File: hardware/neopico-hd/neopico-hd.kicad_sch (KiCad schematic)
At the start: 25 parts, among them J1 HDMI_A, J2 Conn_02x05_Top_Bottom, J4 Audio, J5 AUX, J6 Conn_01x02_Pin, SW1 MENU, SW2 BACK, U1 A_BUFF, U2 V_BUFF, U3 RG_LVS, U4 GB_LVS, U5 AV_LVS

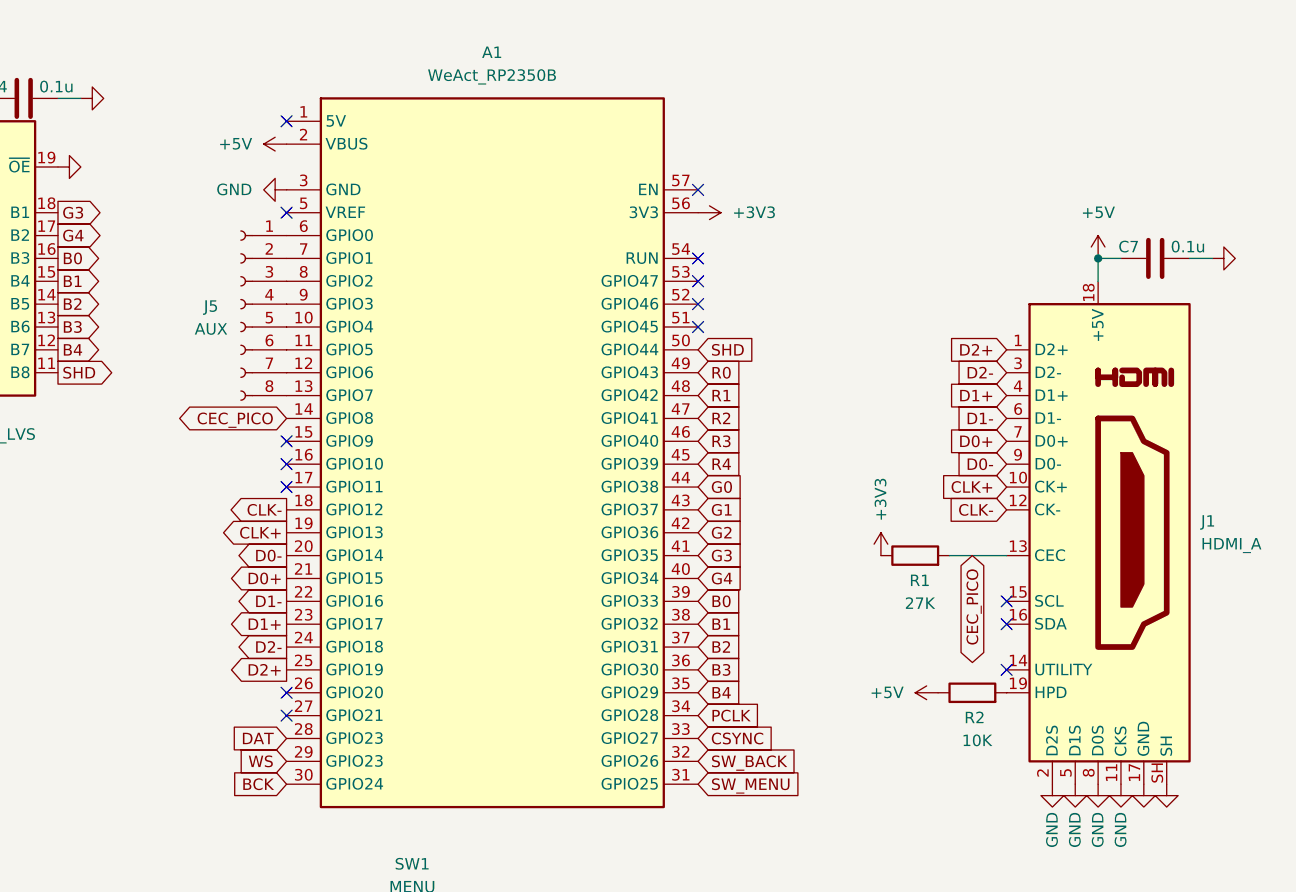
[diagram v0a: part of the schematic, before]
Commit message: Hardware - add HDMI termination resistors and more
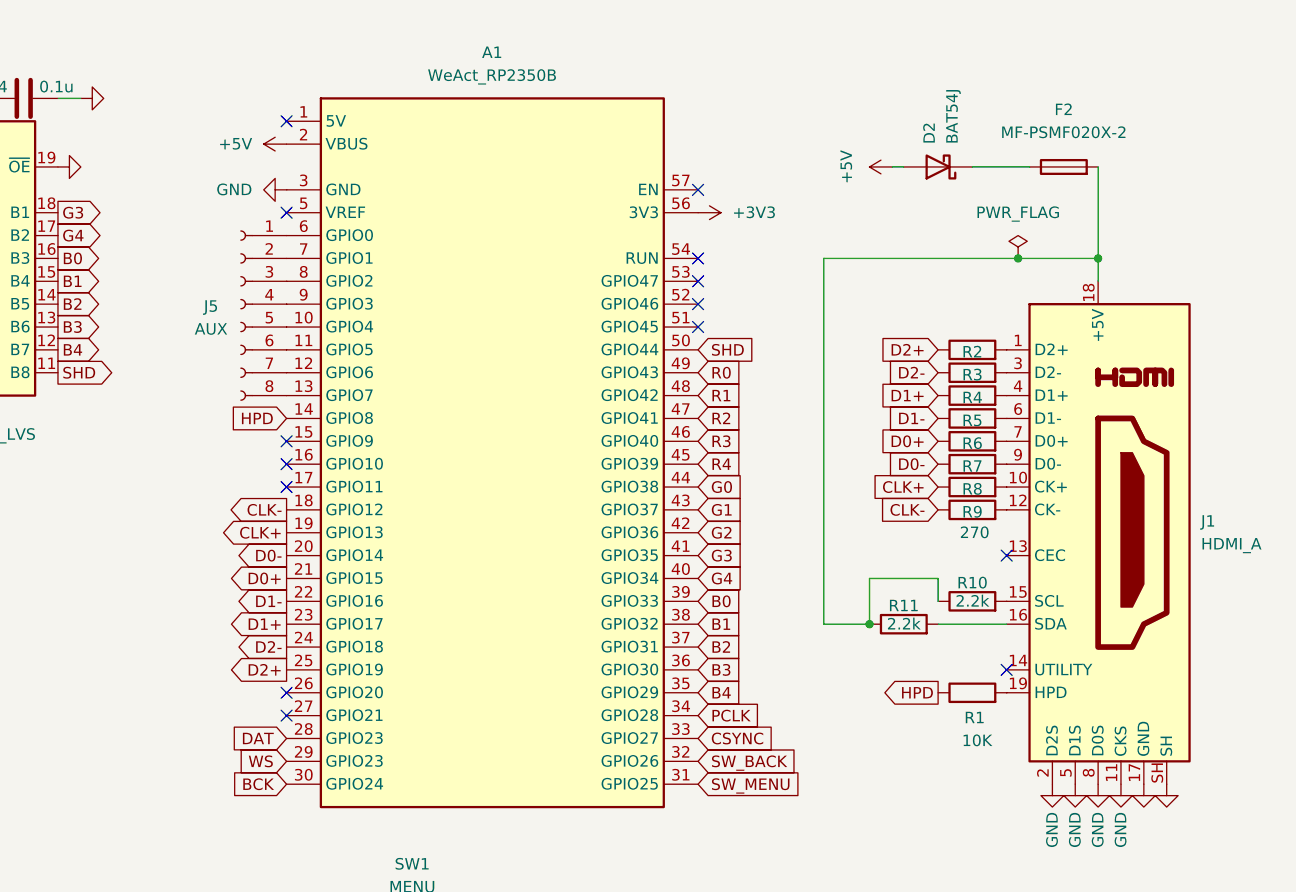
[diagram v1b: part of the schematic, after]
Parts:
- removed C7: 0.1u, Capacitor_SMD:C_0805_2012Metric_Pad1.18x1.45mm_HandSolder, symbol Device:C
- removed R1: 27K, Resistor_SMD:R_0805_2012Metric, symbol Device:R
- added D2: BAT54J, Diode_SMD:D_SOD-323F, symbol Diode:BAT54J
- added F2: MF-PSMF020X-2, Fuse:Fuse_0805_2012Metric, symbol Device:Fuse
- added R10, R11: 2.2k, Resistor_SMD:R_0603_1608Metric, symbol Device:R
- added R2, R3, R4, R5, R6, R7, R8, R9: 270, Resistor_SMD:R_0402_1005Metric, symbol Device:R
- R1: renamed from R2; footprint Resistor_SMD:R_0805_2012Metric_Pad1.20x1.40mm_HandSolder -> Resistor_SMD:R_0603_1608Metric
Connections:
- net +5V: now also D2.2 (A); no longer J1.18 (+5V), R1.1
- net CLK+: now also R8.1; no longer J1.10 (CK+)
- net CLK-: now also R9.1; no longer J1.12 (CK-)
- net D0+: now also R6.1; no longer J1.7 (D0+)
- net D0-: now also R7.1; no longer J1.9 (D0-)
- net D1+: now also R4.1; no longer J1.4 (D1+)
- net D1-: now also R5.1; no longer J1.6 (D1-)
- net D2+: now also R2.1; no longer J1.1 (D2+)
- net D2-: now also R3.1; no longer J1.3 (D2-)
- net at J1.15 (SCL): now also R10.2
- net at J1.16 (SDA): now also R11.2
- net CEC_PICO: no longer names the net of J1.13 (CEC)
- net CEC_PICO: no longer A1.14 (GPIO8)
- new net: J1.10 (CK+), R8.2
- new net: F2.2, J1.18 (+5V), R10.1, R11.1
- new net: J1.1 (D2+), R2.2
- new net: J1.6 (D1-), R5.2
- new net: D2.1 (K), F2.1
- new net: J1.9 (D0-), R7.2
- new net: J1.4 (D1+), R4.2
- new net: J1.7 (D0+), R6.2
- new net: J1.12 (CK-), R9.2
- new net: J1.3 (D2-), R3.2
- new net HPD: A1.14 (GPIO8), R1.1
- no-connect marks 31 -> 30

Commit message: Minor hardware tweaks
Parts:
- C6: footprint Capacitor_THT:CP_Radial_D5.0mm_P2.00mm -> Capacitor_SMD:CP_Elec_6.3x5.4_Nichicon
- D1: LCSC (none) -> C83852
- D2: LCSC (none) -> C86299
- F1: value Polyfuse -> MF-PSMF020X-2; symbol Device:Polyfuse -> Device:Fuse; LCSC (none) -> C89657
- F2: LCSC (none) -> C89657
- FB1: LCSC (none) -> C76815
- J4: footprint Connector_JST:JST_XA_B03B-XASK-1_1x03_P2.50mm_Vertical -> Connector_JST:JST_XA_B04B-XASK-1_1x04_P2.50mm_Vertical; symbol Connector_Generic:Conn_01x03 -> Connector_Generic:Conn_01x04
- R1: LCSC (none) -> C98220
- R10, R11: LCSC (none) -> C114662
- R2, R3, R4, R5, R6, R7, R8, R9: LCSC (none) -> C163474
- SW1, SW2: footprint Connector_Samtec_HPM_THT:Samtec_HPM-02-01-x-S_Straight_1x02_Pitch5.08mm -> Button_Switch_SMD:SW_SPST_CK_KXT3
- U1: value A_BUFF -> SN74LVC2G14DBV; LCSC (none) -> C12401
- U2: value V_BUFF -> SN74LVC2G14DBV; LCSC (none) -> C12401
- U3: value RG_LVS -> SN74LVC245APW; LCSC (none) -> C7848
- U4: value GB_LVS -> SN74LVC245APW; LCSC (none) -> C7848
- U5: value AV_LVS -> SN74LVC245APW; LCSC (none) -> C7848
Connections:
- net GND: now also J2.20 (Pin_20), J4.1 (Pin_1)
- net MVS_BCK: now also J4.2 (Pin_2); no longer J4.1 (Pin_1)
- net MVS_DAT: now also J4.4 (Pin_4); no longer J4.3 (Pin_3)
- net MVS_WS: now also J4.3 (Pin_3); no longer J4.2 (Pin_2)
- net MVS_DARK: now reaches J2.17 (Pin_17)
- net MVS_DARK: now also A1.51 (GPIO45)
- no-connect marks 30 -> 27

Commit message: Update PCB
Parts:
- A1, J2, J4, J5, J6, SW1, SW2: now left out of the parts list
- C1, C2, C3, C4, C5: LCSC (none) -> C1711
- C6: LCSC (none) -> C7094687
- J1: LCSC (none) -> C111617; now left out of the parts list
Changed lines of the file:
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@@
 			)
 		)
+		(property "LCSC" "C1711"
+			(at 100.33 66.04 90)
+			(effects
+				(font
+					(size 1.27 1.27)
+				)
+				(hide yes)
+			)
+		)
 		(pin "1"
 		)
@@
 		(unit 1)
 		(exclude_from_sim no)
-		(in_bom yes)
+		(in_bom no)
 		(on_board yes)
 		(dnp no)
@@
 			)
 		)
+		(property "LCSC" "C1711"
+			(at 52.07 91.44 90)
+			(effects
+				(font
+					(size 1.27 1.27)
+				)
+				(hide yes)
+			)
+		)
 		(pin "1"
 		)
@@
 			)
 		)
+		(property "LCSC" "C7094687"
+			(at 73.66 179.07 0)
+			(effects
+				(font
+					(size 1.27 1.27)
+				)
+				(hide yes)
+			)
+		)
 		(pin "1"
 		)
@@
 		(unit 1)
 		(exclude_from_sim no)
-		(in_bom yes)
+		(in_bom no)
 		(on_board yes)
 		(dnp no)
@@
 		(unit 1)
 		(exclude_from_sim no)
-		(in_bom yes)
+		(in_bom no)
 		(on_board yes)
 		(dnp no)
@@
 			)
 		)
+		(property "LCSC" "C1711"
+			(at 100.33 96.52 90)
+			(effects
+				(font
+					(size 1.27 1.27)
+				)
+				(hide yes)
+			)
+		)
 		(pin "1"
 		)
@@
 			)
 		)
+		(property "LCSC" "C1711"
+			(at 96.52 21.59 90)
+			(effects
+				(font
+					(size 1.27 1.27)
+				)
+				(hide yes)
+			)
+		)
 		(pin "1"
 		)
@@
 			)
 		)
+		(property "LCSC" "C1711"
+			(at 144.78 21.59 90)
+			(effects
+				(font
+					(size 1.27 1.27)
+				)
+				(hide yes)
+			)
+		)
 		(pin "1"
 		)
@@
 		(unit 1)
 		(exclude_from_sim no)
-		(in_bom yes)
+		(in_bom no)
 		(on_board yes)
 		(dnp no)
@@
 		(unit 1)
 		(exclude_from_sim no)
-		(in_bom yes)
+		(in_bom no)
 		(on_board yes)
 		(dnp no)
@@
 		(unit 1)
 		(exclude_from_sim no)
-		(in_bom yes)
+		(in_bom no)
 		(on_board yes)
 		(dnp no)
@@
 		(unit 1)
 		(exclude_from_sim no)
-		(in_bom yes)
+		(in_bom no)
 		(on_board yes)
 		(dnp no)
@@
 		(unit 1)
 		(exclude_from_sim no)
-		(in_bom yes)
+		(in_bom no)
 		(on_board yes)
 		(dnp no)
@@
 			(at 264.16 69.85 0)
 			(effects
+				(font
+					(size 1.27 1.27)
+				)
+				(hide yes)
+			)
+		)
+		(property "LCSC" "C111617"
+			(at 264.16 69.85 0)
+			(effects

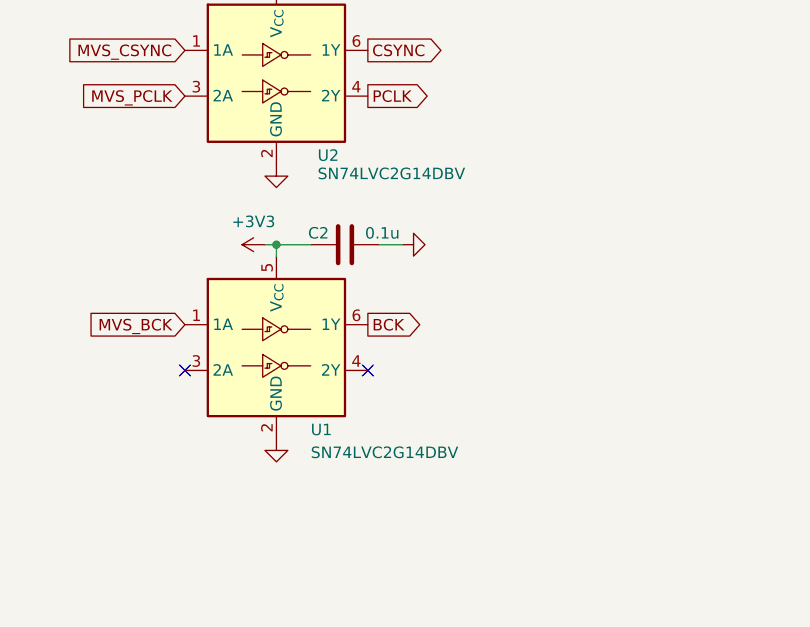
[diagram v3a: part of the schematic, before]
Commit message: Add stable 720p non-RT build
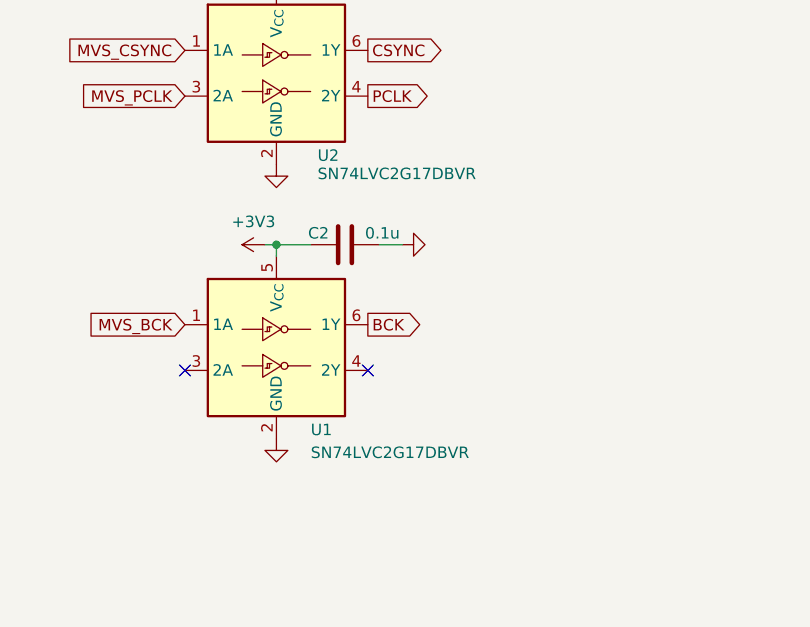
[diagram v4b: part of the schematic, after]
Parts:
- U1, U2: value SN74LVC2G14DBV -> SN74LVC2G17DBVR
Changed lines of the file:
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@@
 			)
 		)
-		(property "Value" "SN74LVC2G14DBV"
+		(property "Value" "SN74LVC2G17DBVR"
 			(at 97.282 88.646 0)
 			(effects
@@
 			)
 		)
-		(property "Value" "SN74LVC2G14DBV"
+		(property "Value" "SN74LVC2G17DBVR"
 			(at 96.52 119.634 0)
 			(effects
